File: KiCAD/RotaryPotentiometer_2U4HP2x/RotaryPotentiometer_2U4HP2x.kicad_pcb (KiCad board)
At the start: 2 copper layers, 20 x 84 mm, 6 parts, among them J1 Conn_01x03_Socket, J2 Conn_01x03_Socket

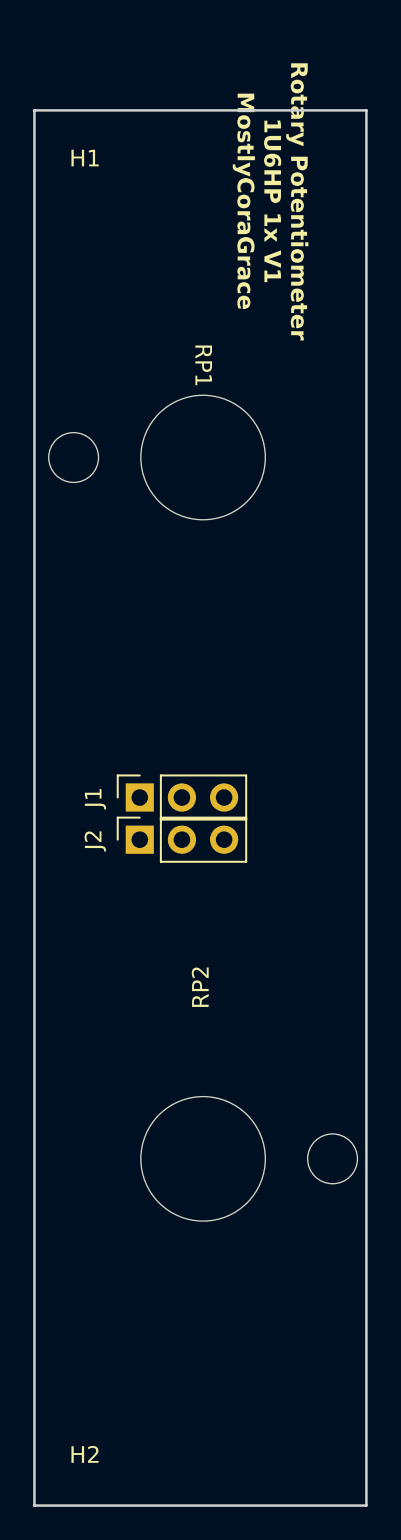
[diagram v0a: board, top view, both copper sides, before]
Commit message: removed all front silkscreen, and flipped most modules, to make the boards 'cleaner'.
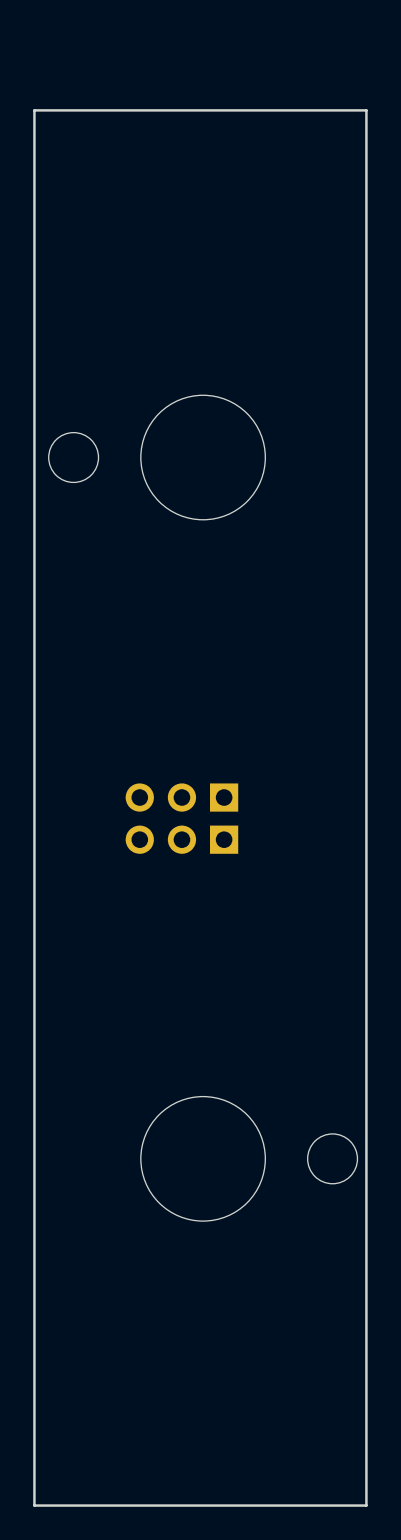
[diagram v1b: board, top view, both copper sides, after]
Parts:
- H1, H2, J1, J2: moved to B.Cu
- moved J1 5.08 mm to (11.4, 43.8)
- moved J2 5.08 mm to (11.4, 46.4)
- turned H1 to 180 degrees
- turned H2 to 180 degrees

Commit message: added copper fills to every module, to maybe possibly increase structural rigidity.
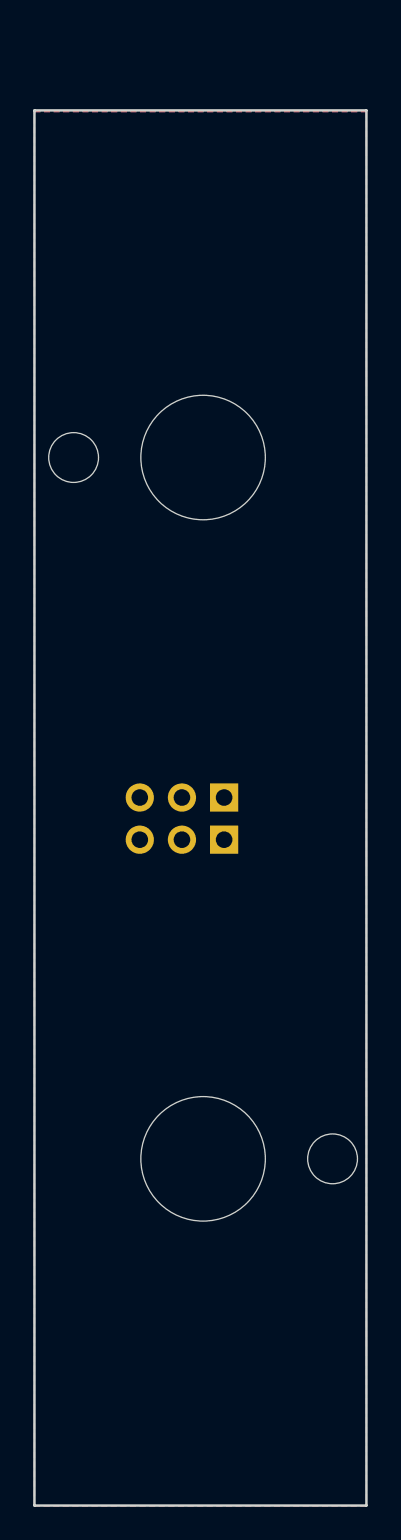
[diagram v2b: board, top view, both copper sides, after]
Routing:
- added copper zone on B.Cu, net (none)
- added copper zone on F.Cu, net (none)
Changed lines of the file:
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@@
+		)
+	)
+	(zone
+		(net 0)
+		(net_name "")
+		(layers "F&B.Cu")
+		(hatch edge 0.5)
+		(connect_pads
+			(clearance 0.5)
+		)
+		(min_thickness 0.25)
+		(filled_areas_thickness no)
+		(fill yes
+			(thermal_gap 0.5)
+			(thermal_bridge_width 0.5)
+			(island_removal_mode 1)
+			(island_area_min 10)
+		)
+		(polygon
+			(pts
+				(xy 0 2.5) (xy 20 2.5) (xy 20 86.5) (xy 0 86.5)
+			)
 		)
 	)
